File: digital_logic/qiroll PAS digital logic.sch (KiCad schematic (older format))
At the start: 9 parts, among them U1 14538, U2 4012, U3 4027, U4 14538

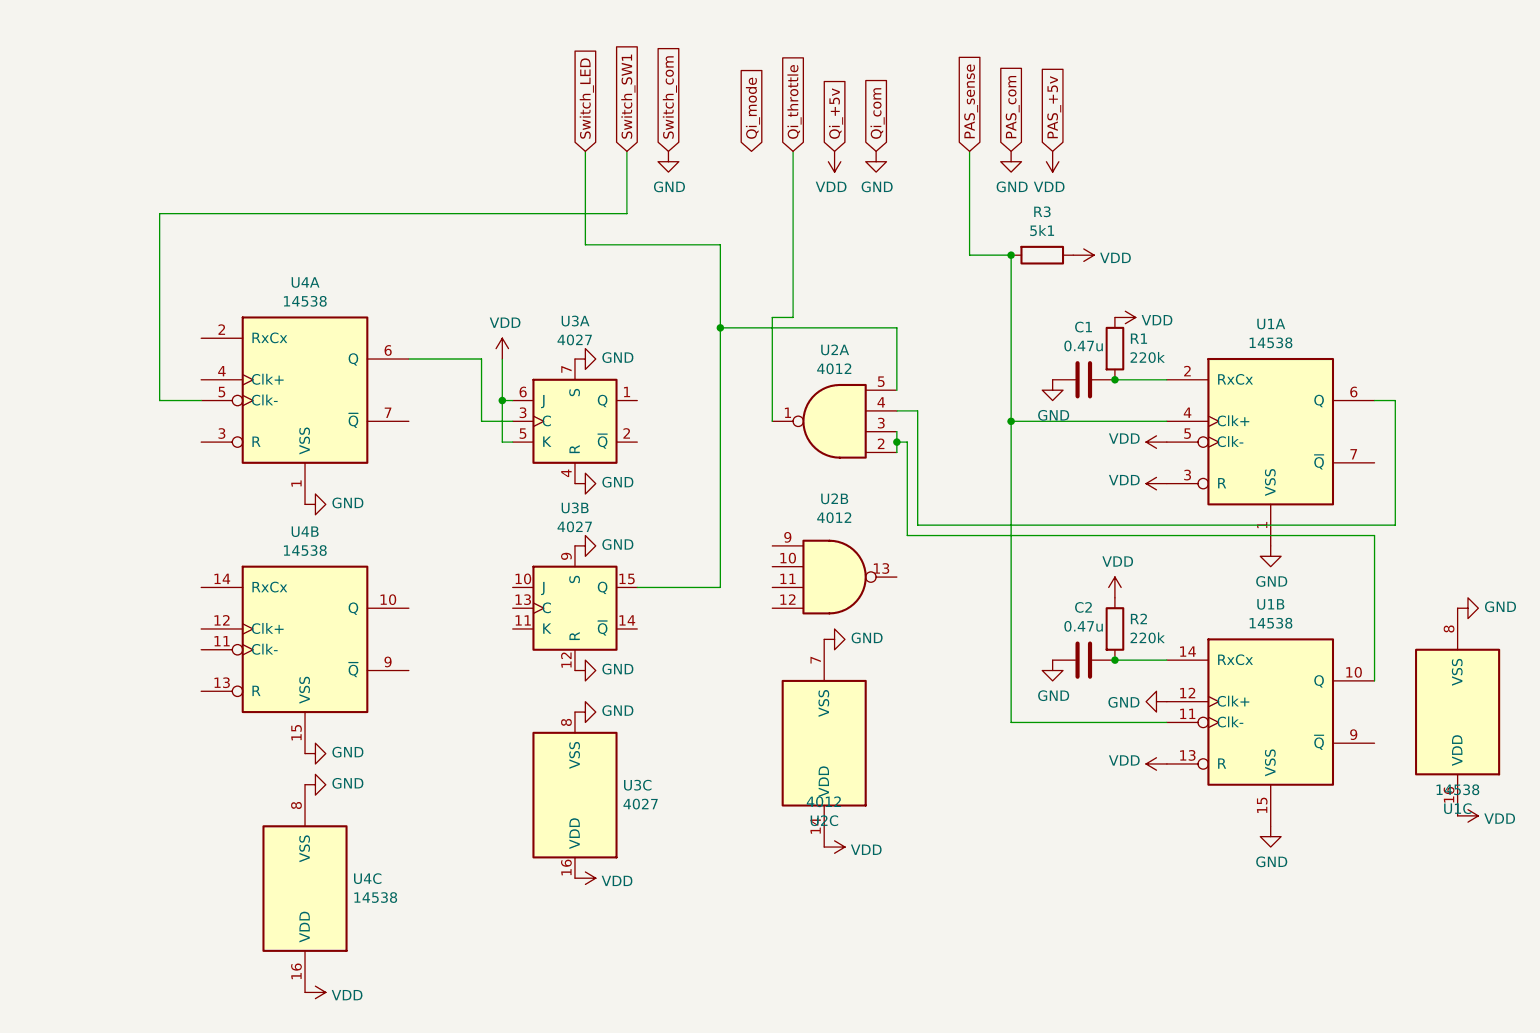
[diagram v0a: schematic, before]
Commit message: digital logic prototype kicad schematic, complete but untested
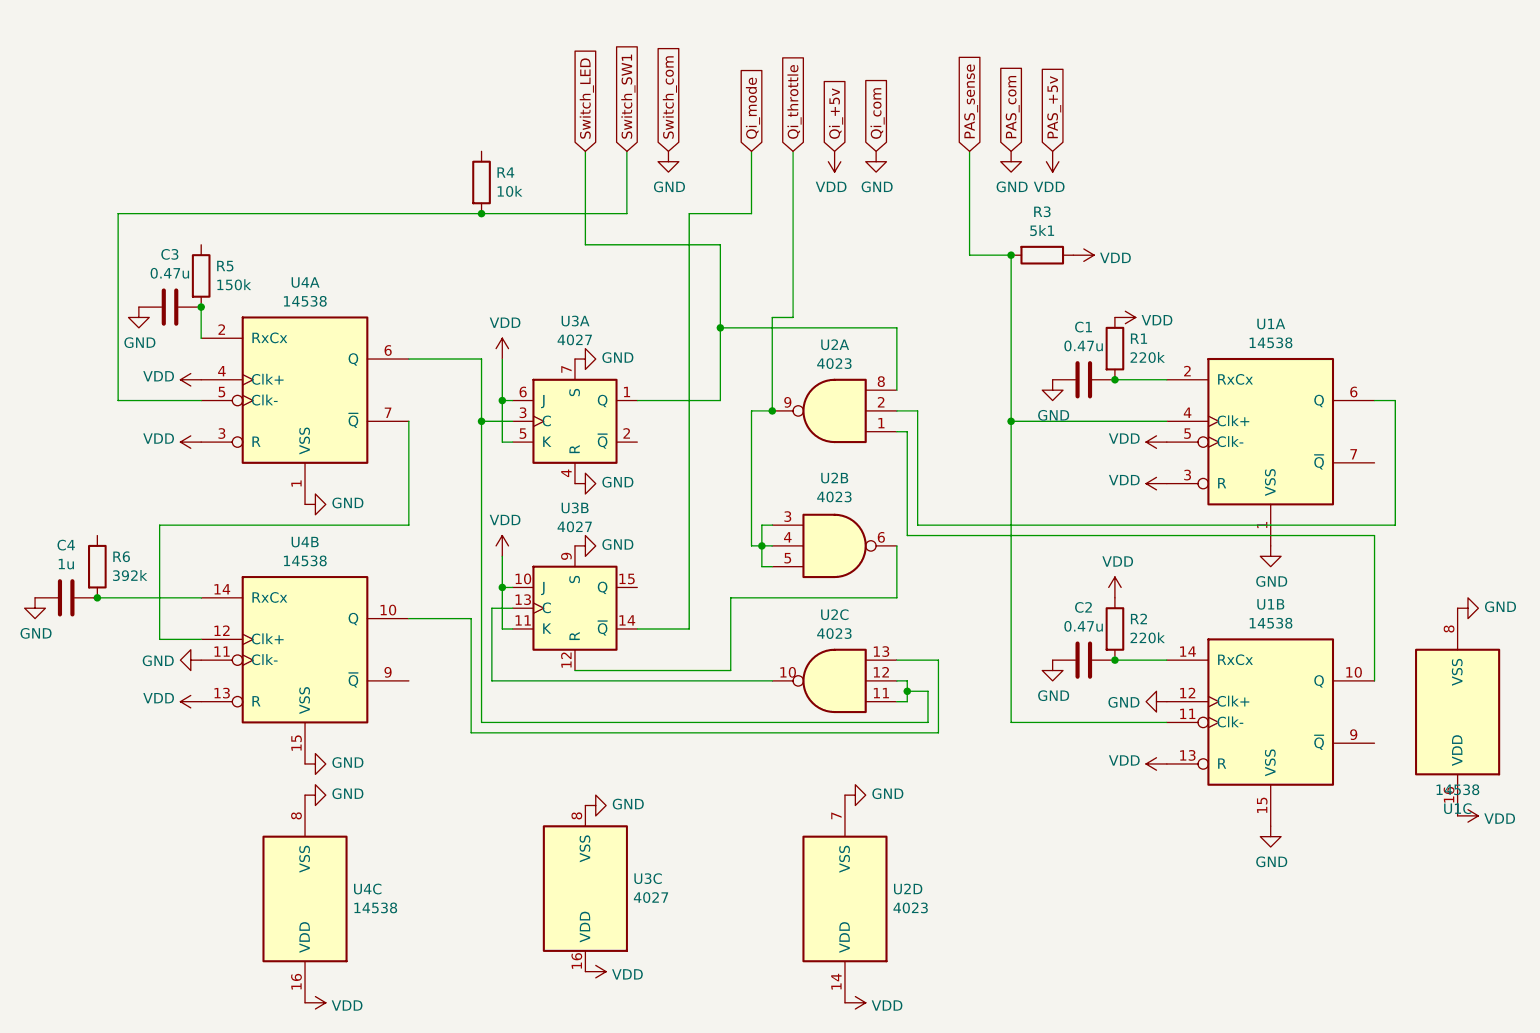
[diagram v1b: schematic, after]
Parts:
- removed U2: 4012, symbol 4xxx:4012
- added C3: 0.47u, symbol Device:C
- added C4: 1u, symbol Device:C
- added R4: 10k, symbol Device:R
- added R5: 150k, symbol Device:R
- added R6: 392k, symbol Device:R
- added U2: 4023, symbol 4xxx:4023
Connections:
- net GND: now also U4.11 (Clk-), C3.2, C4.2, U2.7 (VSS); no longer U3.12 (R)
- net Qi_mode: now also U3.14 (~Q)
- net Qi_throttle: now also U2.3, U2.4, U2.5, U2.9
- net Switch_LED: now also U3.1 (Q), U2.8; no longer U3.15 (Q)
- net Switch_SW1: now also R4.2
- net VDD: now also U3.10 (J), U3.11 (K), U4.13 (R), U4.3 (R), U4.4 (Clk+), U2.14 (VDD)
- net at U1.6 (Q): now also U2.2
- net at U1.10 (Q): now also U2.1
- net at U3.3 (C), U4.6 (Q): now also U2.11, U2.12
- net at U3.13 (C): now also U2.10
- net at U4.2 (RxCx): now also C3.1, R5.2
- net at U4.7 (~Q): now also U4.12 (Clk+)
- net at U4.10 (Q): now also U2.13
- net at U4.14 (RxCx): now also C4.1, R6.2
- new net: U2.6, U3.12 (R)
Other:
- moved on the sheet: U3C, U4B, U4C
